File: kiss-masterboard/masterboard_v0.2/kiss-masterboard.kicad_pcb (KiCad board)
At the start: 2 copper layers, 187 x 152 mm, 162 parts, among them J1 Cubebatt_host, J10 CRESET, J11 Jumper, J12 Jumper, J13 Conn_02x08_Odd_Even, J14 Conn_02x08_Odd_Even, J15 jmp, J16 jmp, J2 Conn_01x02, J3 Conn_01x02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

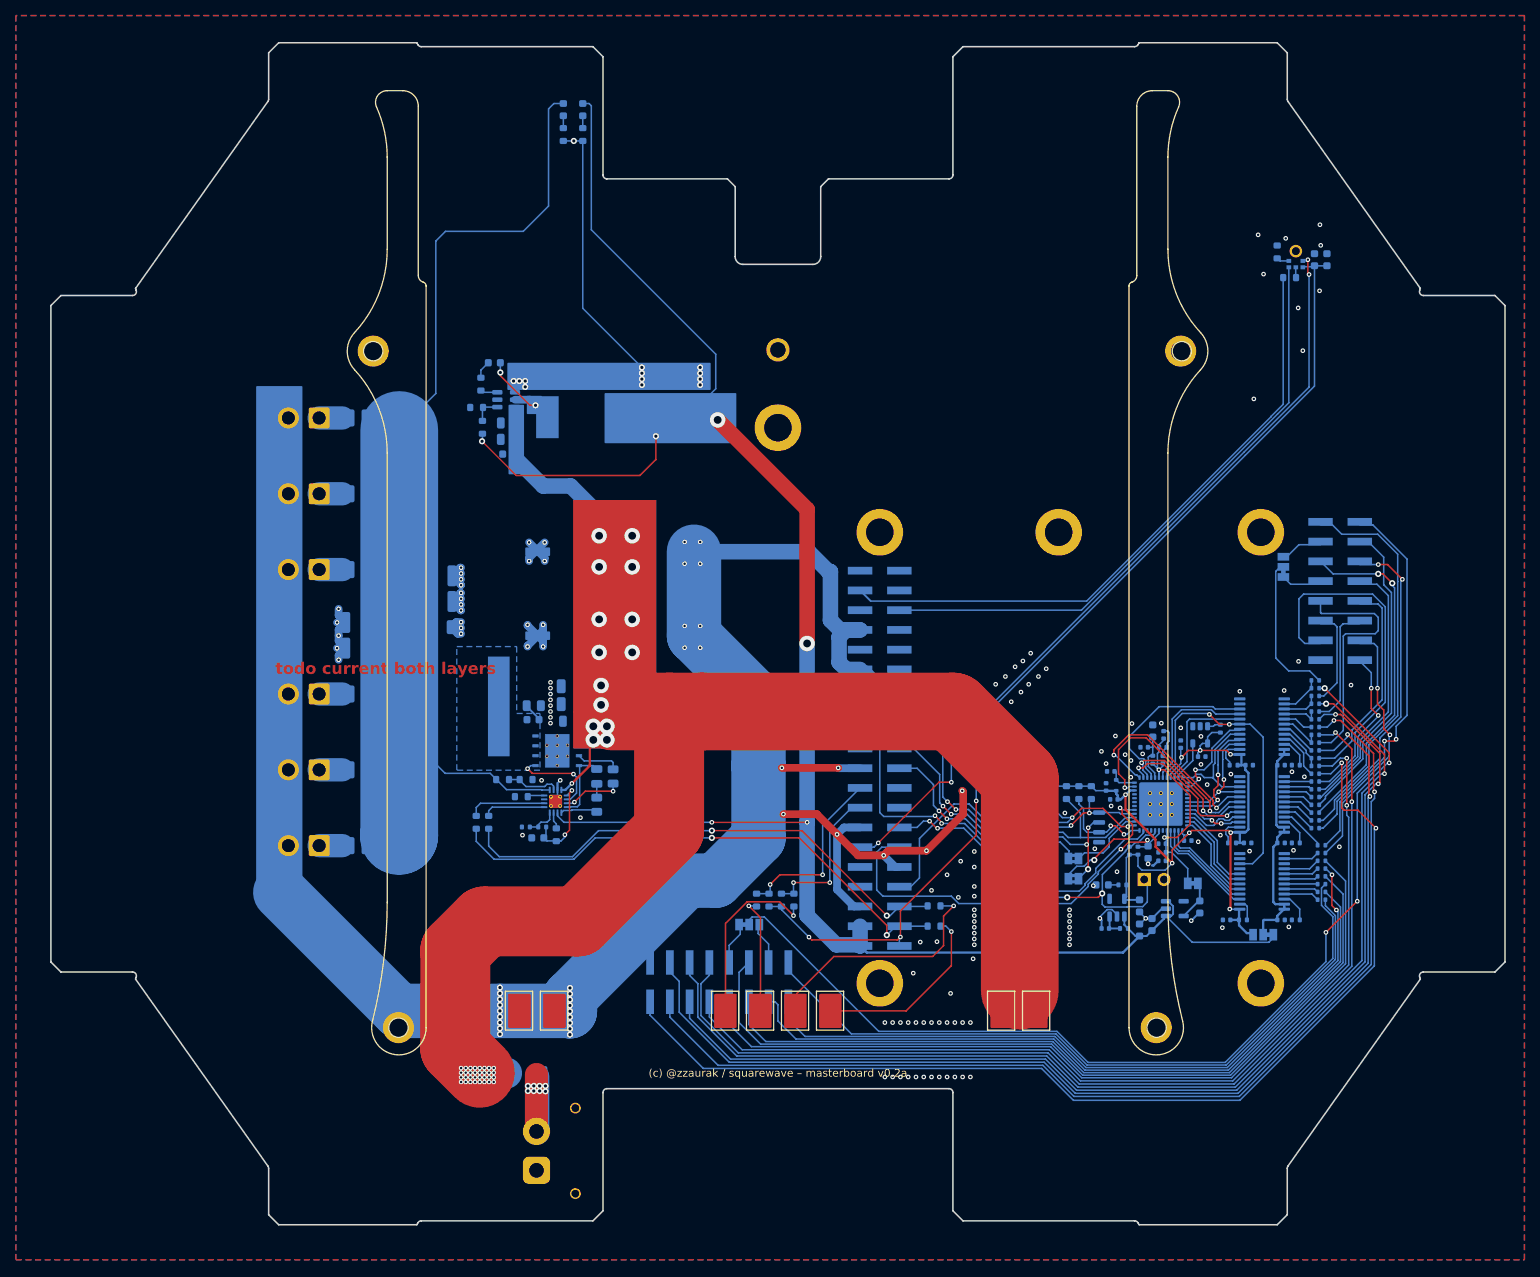
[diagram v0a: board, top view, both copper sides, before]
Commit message: Add extension header
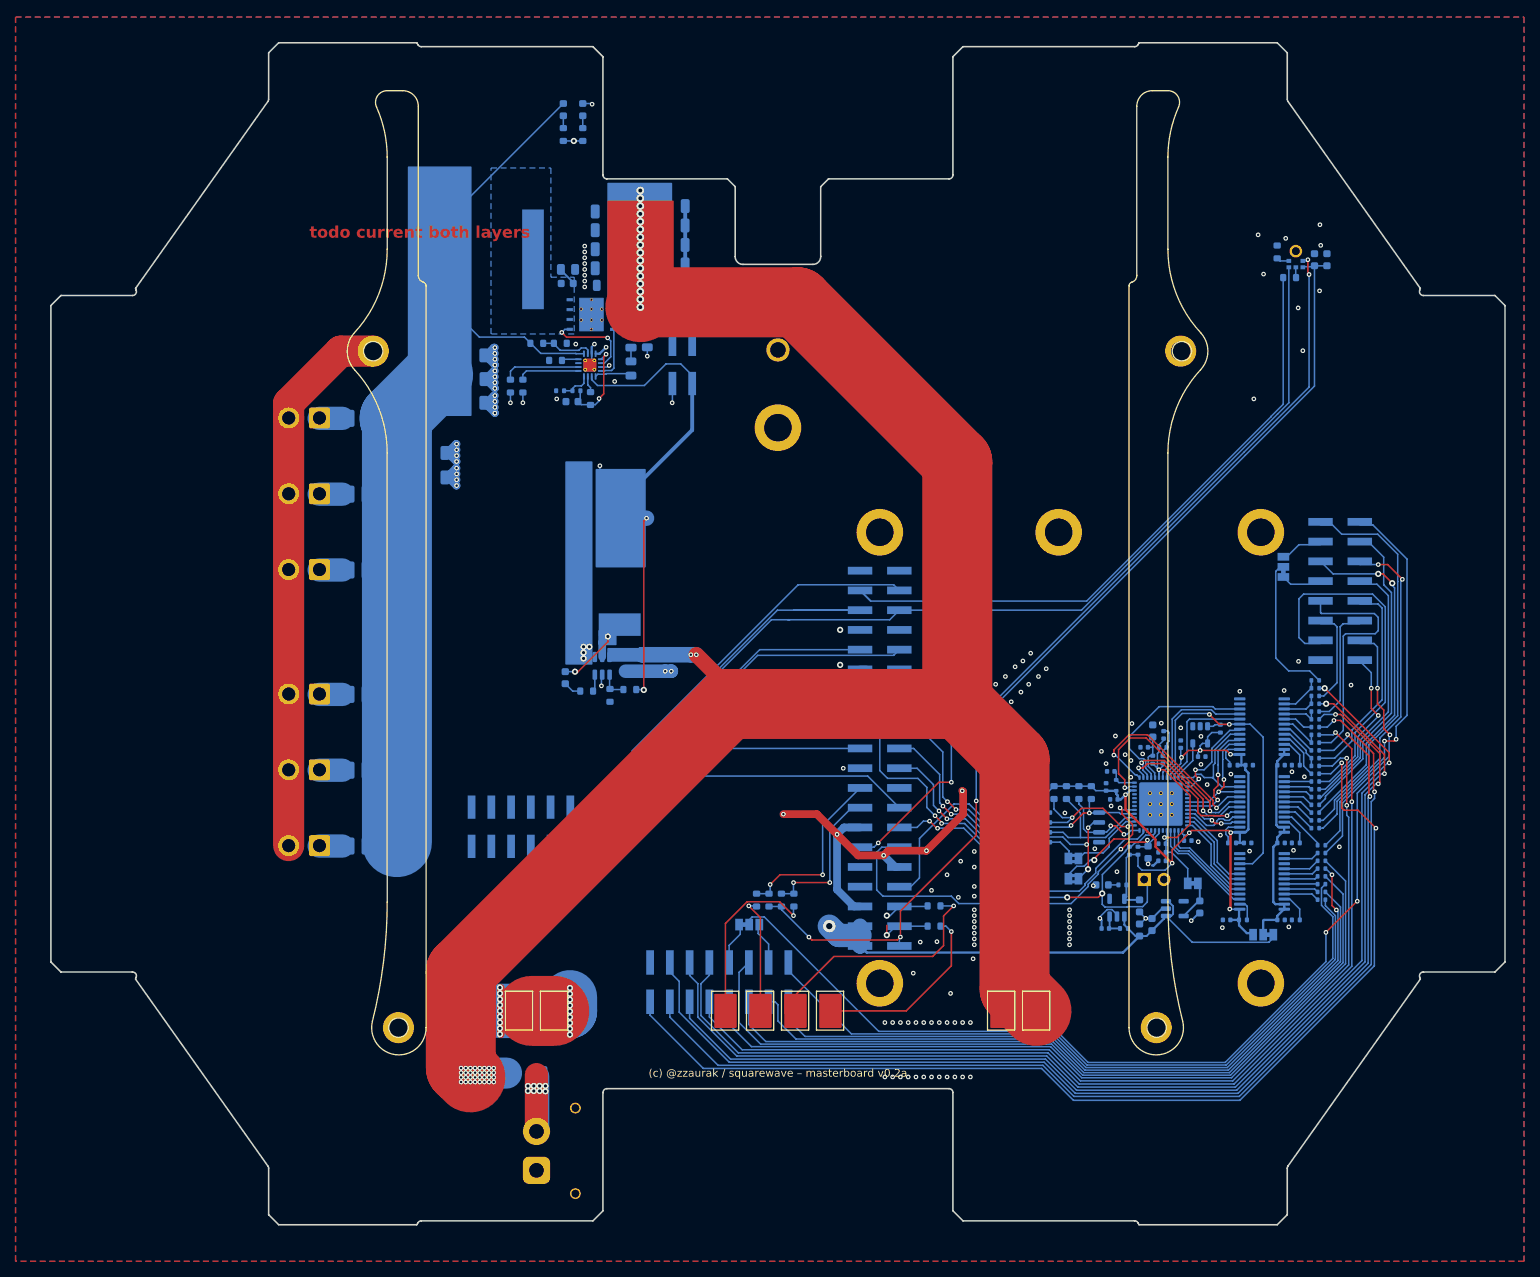
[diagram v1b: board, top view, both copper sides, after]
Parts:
- removed C47, C49, C51: 47µF, Capacitor_SMD:C_1210_3225Metric
- added C55: 22uF, Capacitor_SMD:C_1206_3216Metric, B.Cu at (94.6, 42.0)
- added C59: 22uF, Capacitor_SMD:C_1206_3216Metric, B.Cu at (94.6, 46.8)
- added C60: 22uF, Capacitor_SMD:C_1206_3216Metric, B.Cu at (94.6, 34.5)
- added C62: 22uF, Capacitor_SMD:C_1206_3216Metric, B.Cu at (86.0, 35.2)
- added C63: 47uF, Capacitor_SMD:C_1206_3216Metric, B.Cu at (63.7, 69.4)
- added C64: 47uF, Capacitor_SMD:C_1206_3216Metric, B.Cu at (68.7, 59.8)
- added C65: 47uF, Capacitor_SMD:C_1206_3216Metric, B.Cu at (68.7, 56.8)
- added J17: Conn_02x05_Counter_Clockwise, Connector_PinSocket_2.54mm:PinSocket_2x06_P2.54mm_Vertical_SMD, B.Cu at (75.0, 114.3)
- added J18: Conn_02x02_Counter_Clockwise, Connector_PinSocket_2.54mm:PinSocket_2x02_P2.54mm_Vertical_SMD, B.Cu at (95.7, 54.8)
- C46, C48, C50, C52: value 47µF -> 22uF; footprint Power_Board:CP_OSCON_Poly_F12 -> Capacitor_SMD:C_1206_3216Metric
- C53: value 47µF -> 47uF; footprint Capacitor_SMD:C_1210_3225Metric -> Capacitor_SMD:C_1206_3216Metric
- J2, J3, J4, J5, J6, J7: moved to F.Cu
- moved L1 57.7 mm to (71.1, 41.4)
- moved C44 56.4 mm to (86.0, 40.0)
- moved C40 56.3 mm to (81.5, 59.6)
- moved R36 56.3 mm to (79.4, 54.4)
- moved R42 56.3 mm to (81.0, 42.6)
- moved R43 56.3 mm to (77.0, 52.1)
- moved R44 56.3 mm to (80.0, 52.1)
- moved R7 56.3 mm to (75.2, 57.6)
- moved R8 56.3 mm to (73.6, 57.6)
- moved C41 56.3 mm to (89.1, 51.8)
- moved C42 56.3 mm to (80.9, 44.5)
- moved R37 56.3 mm to (82.1, 58.2)
- moved R38 56.3 mm to (80.0, 58.2)
- moved R39 56.3 mm to (83.9, 59.2)
- moved R40 56.3 mm to (89.1, 55.4)
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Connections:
- P2 pad 15: unconnected-(P2-P15-Pad15) -> /Raspberry Pi/GPIO_22
- P2 pad 22: unconnected-(P2-P22-Pad22) -> /Raspberry Pi/GPIO_25
- P2 pad 29: unconnected-(P2-P29-Pad29) -> /Raspberry Pi/GPIO_5
- P2 pad 31: unconnected-(P2-P31-Pad31) -> /Raspberry Pi/GPIO_6
- P2 pad 32: unconnected-(P2-P32-Pad32) -> /Raspberry Pi/GPIO_12
- P2 pad 36: unconnected-(P2-P36-Pad36) -> /Raspberry Pi/GPIO_16
- P2 pad 37: unconnected-(P2-P37-Pad37) -> /Raspberry Pi/GPIO_26
- U3 pad 5: unconnected-(U3-EN-Pad5) -> /RaspiPower/Power_EN
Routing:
- net GND: track 316.2 -> 227.9 mm, vias 188 -> 171
- net /Power+: track 198.7 -> 251.7 mm, vias 47 -> 51
- net /Raspberry Pi/GPIO_16: track 0.00 -> 44.8 mm
- net /RaspiPower/Power_EN: track 0.00 -> 44.1 mm, vias 0 -> 2
- net /Raspberry Pi/GPIO_26: track 0.00 -> 43.6 mm
- net /Digital Audio/LRCLK: track 78.6 -> 119.6 mm
- net /Raspberry Pi/GPIO_12: track 0.00 -> 35.8 mm
- net /Raspberry Pi/GPIO_6: track 0.00 -> 34.1 mm
- net /Raspberry Pi/GPIO_22: track 0.00 -> 33.6 mm
- net /Digital Audio/BCLK: track 102.2 -> 134.7 mm
- net /Raspberry Pi/GPIO_5: track 0.00 -> 31.8 mm
- net /SCL: track 65.5 -> 93.7 mm
- net /Raspberry Pi/GPIO_25: track 0.00 -> 25.1 mm
- net /5V_switched: track 259.7 -> 235.3 mm, vias 6 -> 5
- net /SDA: track 68.4 -> 89.9 mm
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- added copper zone on In1.Cu, net GND
- added copper zone on In2.Cu, net GND
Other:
- copper layers 2 -> 4

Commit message: Added IMU, routed extension layer, switched battery polarity
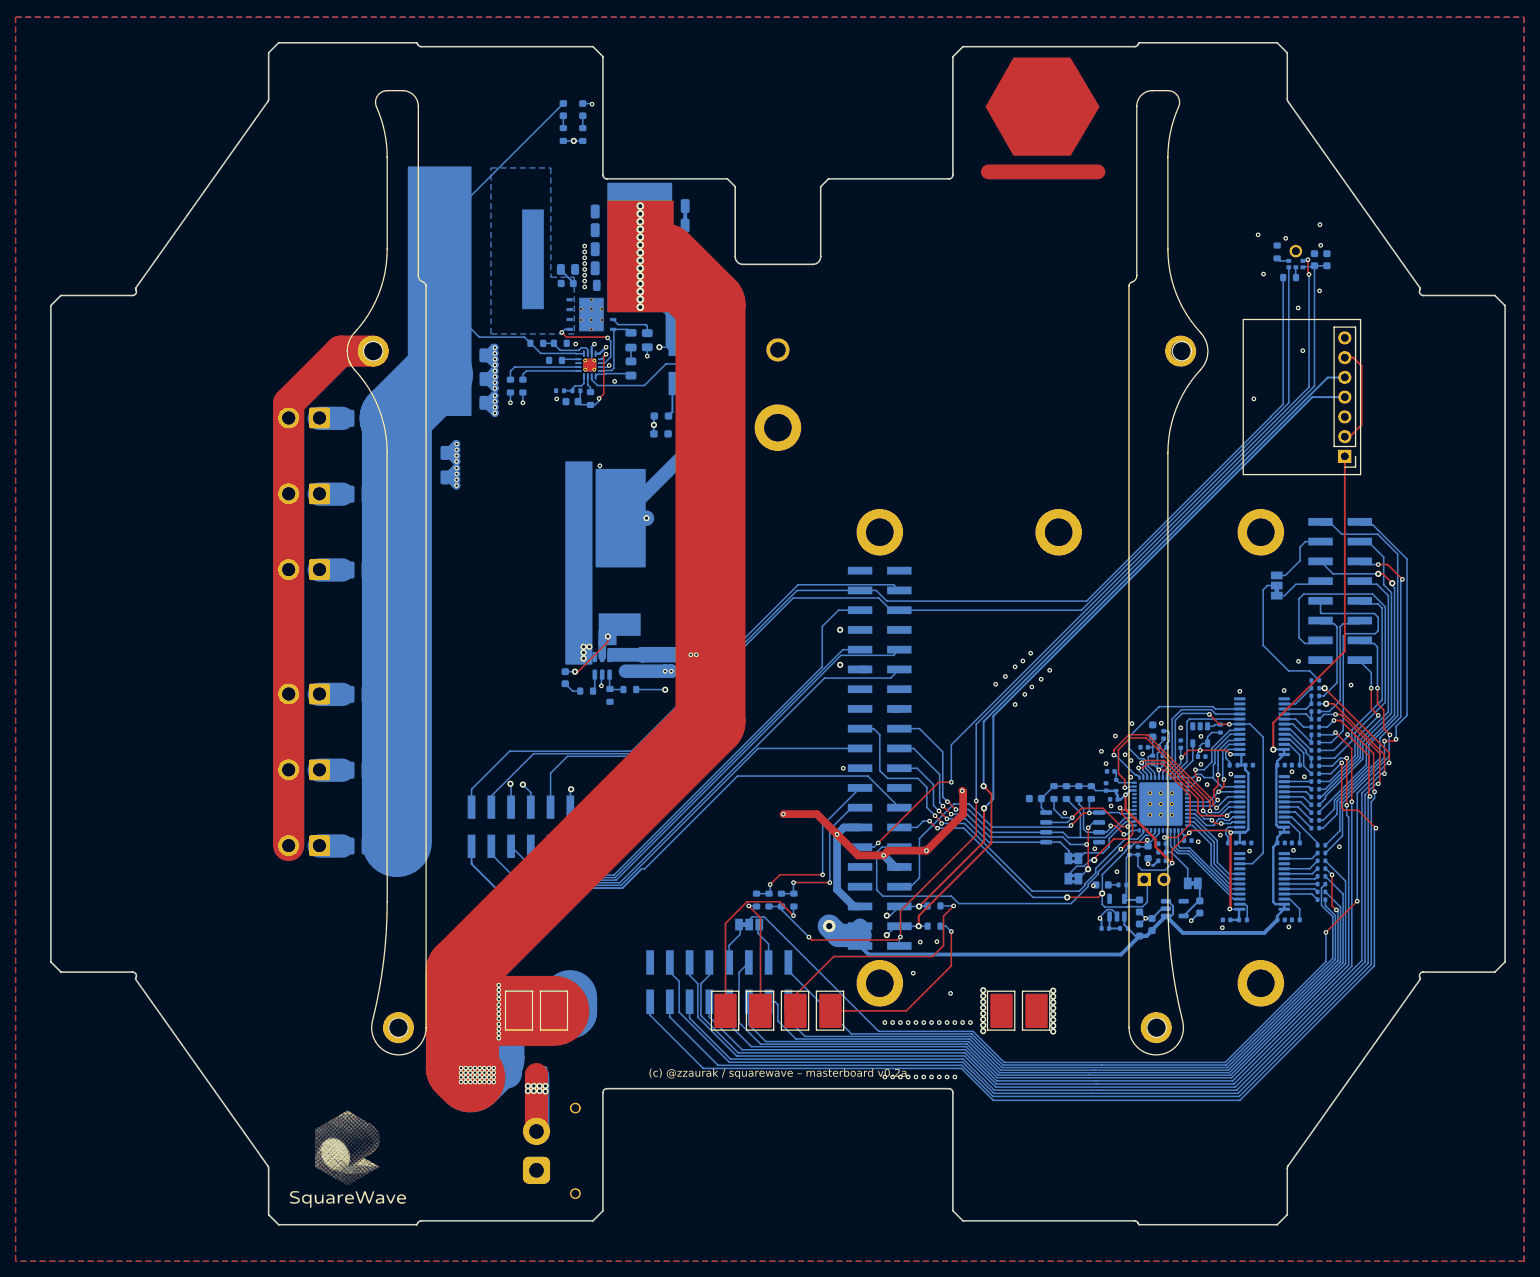
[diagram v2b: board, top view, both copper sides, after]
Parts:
- added LG1: Logo_DOT1, logos:Logo_Dot_15mm_Text_Mask, F.Cu at (142.1, 23.2)
- added LG2: Logo_Squarewave, logos:Logo_Squarewave_Text_15mm_Silks, F.Cu at (52.7, 157.1)
- added R12: 68.8k, Resistor_SMD:R_0603_1608Metric_Pad0.98x0.95mm_HandSolder, B.Cu at (93.0, 63.8)
- added R13: 732k, Resistor_SMD:R_0603_1608Metric_Pad0.98x0.95mm_HandSolder, B.Cu at (93.0, 61.5)
- C1, C2, C43, C44, C45: value 10µF -> 10uF
- C11, C12, C15, C16, C19, C24, C25, C28, C29, C30, C31, C56, C57, C61, C9: value 100n -> 100nF
- C14, C17, C8: value 1u -> 1uF
- C35, C39, C40: value 1µF -> 1uF
- C58, C7: value 22µF -> 22uF; footprint Capacitor_SMD:C_1210_3225Metric -> Capacitor_SMD:C_1206_3216Metric
- J9: value jmp -> Conn_01x07_Pin; footprint Jumper:SolderJumper-3_P1.3mm_Bridged12_Pad1.0x1.5mm -> kiss:PinHeader_1x07_imu; moved to F.Cu
- R14: value 100E -> 100
- R20: value 330E -> 330
- R24: value 2k2 -> 2.2k
- R34: value 10K -> 10k
- R36: value 38.3K -> 38.3k
- R37: value 294K -> 294k
- R39: value 100K -> 100k
- moved J9 62.4 mm to (180.9, 66.7)
- moved J16 2.55 mm to (172.2, 83.3)
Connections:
- net /Raspberry Pi/PCM_DOUT renamed /DIN
- C24 pad 2: /FPGA Panel Driver/VCCB -> /5V_switched
- C31 pad 2: /FPGA Panel Driver/VCCB -> /5V_switched
- C57 pad 2: /FPGA Panel Driver/VCCB -> /5V_switched
- J17 pad 1: /Raspberry Pi/GPIO_12 -> /E_GPIO_22
- J17 pad 10: /Raspberry Pi/GPIO_25 -> /LRCLK
- J17 pad 11: /Raspberry Pi/GPIO_22 -> /E_GPIO_16
- J17 pad 12: /Raspberry Pi/GPIO_16 -> /BCLK
- J17 pad 2: /Raspberry Pi/GPIO_6 -> /E_GPIO_26
- J17 pad 3: /Raspberry Pi/GPIO_5 -> /E_GPIO_25
- J17 pad 4: /SCL -> /DOUT
- J17 pad 5: /SDA -> /E_GPIO_5
- J17 pad 6: unconnected-(J17-Pin_6-Pad6) -> /SDA
- J17 pad 7: /Digital Audio/LRCLK -> /E_GPIO_6
- J17 pad 8: /Digital Audio/BCLK -> /SCL
- J17 pad 9: /Raspberry Pi/GPIO_26 -> /E_GPIO_12
- J9 pad 2: /FPGA Panel Driver/VCCB -> Net-(J9-Pin_2)
- J9 pad 3: +3V3 -> GND
- P2 pad 12: /Digital Audio/BCLK -> /BCLK
- P2 pad 15: /Raspberry Pi/GPIO_22 -> /E_GPIO_22
- P2 pad 22: /Raspberry Pi/GPIO_25 -> /E_GPIO_25
- P2 pad 29: /Raspberry Pi/GPIO_5 -> /E_GPIO_5
- P2 pad 31: /Raspberry Pi/GPIO_6 -> /E_GPIO_6
- P2 pad 32: /Raspberry Pi/GPIO_12 -> /E_GPIO_12
- P2 pad 35: /Digital Audio/LRCLK -> /LRCLK
- P2 pad 36: /Raspberry Pi/GPIO_16 -> /E_GPIO_16
- P2 pad 37: /Raspberry Pi/GPIO_26 -> /E_GPIO_26
- P2 pad 38: /Digital Audio/DOUT -> /DOUT
- R35 pad 1: /Digital Audio/DOUT -> /DOUT
- U13 pad 23: /FPGA Panel Driver/VCCB -> /5V_switched
- U13 pad 24: /FPGA Panel Driver/VCCB -> /5V_switched
- U2 pad 23: /FPGA Panel Driver/VCCB -> /5V_switched
- U2 pad 24: /FPGA Panel Driver/VCCB -> /5V_switched
- U3 pad 5: /RaspiPower/Power_EN -> Net-(U3-EN)
- U5 pad 23: /FPGA Panel Driver/VCCB -> /5V_switched
- U5 pad 24: /FPGA Panel Driver/VCCB -> /5V_switched
- U7 pad 1: /Digital Audio/LRCLK -> /LRCLK
- U7 pad 4: /Digital Audio/BCLK -> /BCLK
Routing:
- net /BCLK: track 0.00 -> 146.9 mm, vias 0 -> 5
- net /DOUT: track 0.00 -> 141.6 mm
- net /LRCLK: track 0.00 -> 137.8 mm
- net /Digital Audio/BCLK: track 134.7 -> 0.00 mm, vias 4 -> 0
- net /SDA: track 89.9 -> 211.3 mm, vias 2 -> 5
- net /Digital Audio/LRCLK: track 119.6 -> 0.00 mm
- net /SCL: track 93.7 -> 204.9 mm, vias 2 -> 5
- net /5V_switched: track 235.3 -> 317.8 mm, vias 5 -> 6
- net /Digital Audio/DOUT: track 81.8 -> 0.00 mm
- net /E_GPIO_26: track 0.00 -> 68.5 mm
- net /Power+: track 251.7 -> 183.3 mm, vias 51 -> 62
- net /E_GPIO_22: track 0.00 -> 66.2 mm
- net /E_GPIO_5: track 0.00 -> 63.2 mm
- net /E_GPIO_6: track 0.00 -> 61.5 mm
- net /E_GPIO_25: track 0.00 -> 57.4 mm
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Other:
- board text added: "For programming iCE cut traces connecting J11 and J12 pads. Short the left pad of J11 and J12, same for the right one"
- board text added: "If no Power Management Extension is used, Pin 1 and 2 (the marked ones) need to be connected, to power up the board"
- board text removed: "Speaker"
- board text removed: "todo current both layers"
